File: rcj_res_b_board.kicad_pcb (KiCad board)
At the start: 2 copper layers, 92.5 x 100 mm, 94 parts, among them P1 GP2Y0A41SK0F, P10 SERVO0, P11 MPU9250, P12 PING0, P13 CONN_01X03, P14 CONN_01X03, P15 CONN_01X04, P16 CONN_02X04, P2 GP2Y0A41SK0F, P3 GP2Y0A41SK0F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

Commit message: Power routing & prep for autoroute
Moved some components to make routing power easier (net ties)
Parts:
- NT2, NT3, NT4: moved to B.Cu
- moved NT3 36.2 mm to (45.0, 67.5)
- moved NT4 35.2 mm to (47.0, 69.0)
- moved NT2 32.8 mm to (47.0, 65.0), turned to 180 degrees
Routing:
- net /3.3V: track 26.8 -> 251.0 mm, vias 0 -> 3
- net GNDD: track 88.1 -> 305.1 mm, vias 1 -> 2
- net GNDA: track 7.82 -> 121.7 mm, vias 1 -> 0
- net GNDPWR: track 50.1 -> 109.1 mm
- net /VBAT1: track 12.8 -> 61.5 mm, vias 0 -> 1
- net Net-(C23-Pad1): track 0.00 -> 4.11 mm
- net Net-(C22-Pad1): track 0.00 -> 3.40 mm
- net Net-(C21-Pad1): track 0.00 -> 3.40 mm
- net GND: track 44.7 -> 42.7 mm

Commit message: Changed grounds
Servo now uses digital ground
Battery monitor uses analog ground
Moved P_PWR1's 3.3V (used for debugging) to debug header
	P_PWR2 -> P_PWR1
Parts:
- removed the P_PWR1 at (89.0, 117.0)
- P_DBG1: value CONN_01X03 -> CONN_01X04; footprint Socket_Strips:Socket_Strip_Straight_1x03 -> Socket_Strips:Socket_Strip_Straight_1x04
- renumbered P_PWR2 to P_PWR1
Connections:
- MCU1 pad 1: Net-(MCU1-Pad1) -> (no net)
- MCU1 pad 15: Net-(MCU1-Pad15) -> (no net)
- MCU1 pad 2: Net-(MCU1-Pad2) -> (no net)
- MCU1 pad 20: Net-(MCU1-Pad20) -> (no net)
- MCU1 pad 36: Net-(MCU1-Pad36) -> (no net)
- MCU1 pad 40: Net-(MCU1-Pad40) -> (no net)
- MCU1 pad 5: Net-(MCU1-Pad5) -> (no net)
- MCU1 pad 53: Net-(MCU1-Pad53) -> (no net)
- MCU1 pad 56: Net-(MCU1-Pad56) -> (no net)
- MCU1 pad 6: Net-(MCU1-Pad6) -> (no net)
- MCU1 pad 62: Net-(MCU1-Pad62) -> (no net)
- P10 pad 1: GNDPWR -> GNDD
- P16 pad 8: Net-(P16-Pad8) -> (no net)
- P_CT1 pad 8: Net-(P_CT1-Pad8) -> (no net)
- P_DBG1 pad 2: /SWDIO -> /3.3V
- P_DBG1 pad 3: /SWCLK -> /SWDIO
- R8 pad 2: GNDD -> GNDA
- REG1 pad 4: Net-(REG1-Pad4) -> (no net)
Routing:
- net GNDPWR: track 109.1 -> 50.1 mm
- net GNDD: track 305.1 -> 269.9 mm
- net /VBAT1: track 61.5 -> 49.1 mm, vias 1 -> 0
- net /3.3V: track 251.0 -> 240.0 mm

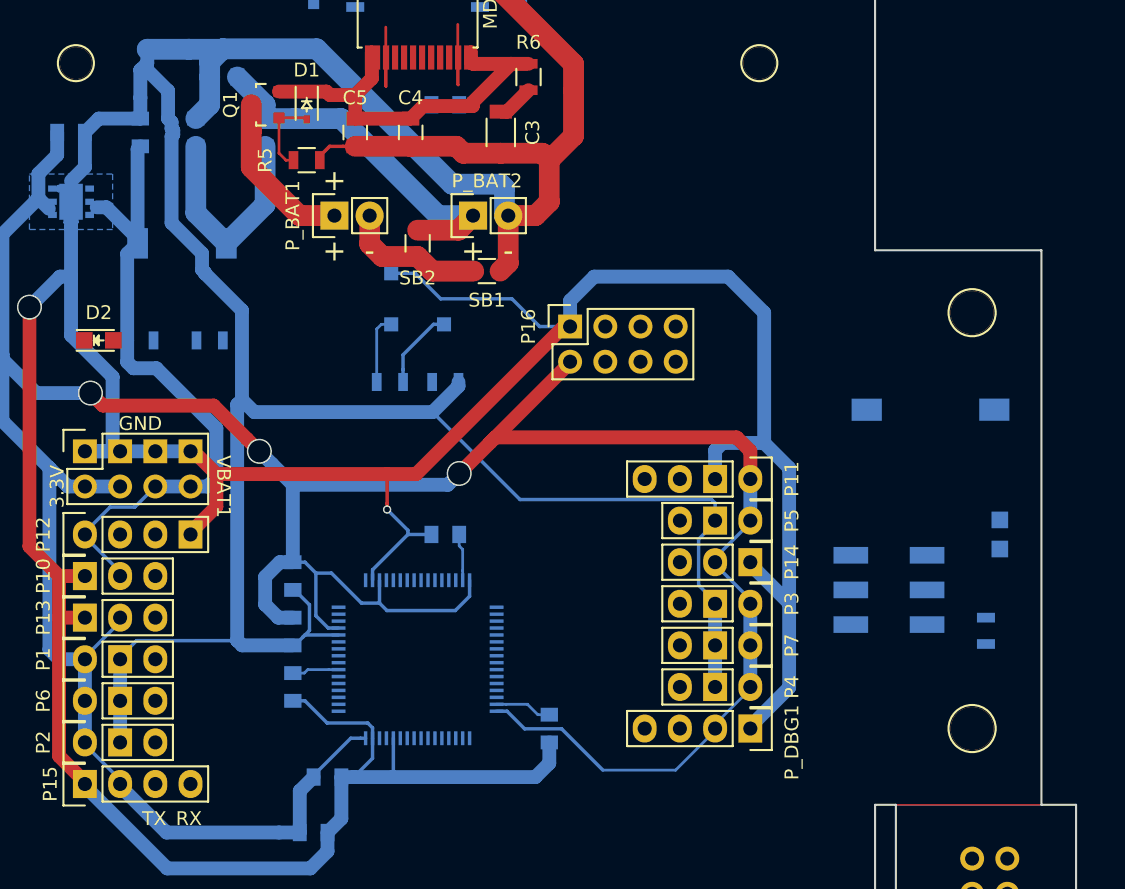
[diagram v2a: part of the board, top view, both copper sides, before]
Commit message: Re-routed power
Removed unnecessary wiring that wasn't power (to let autorouter route instead)
Misc fixes
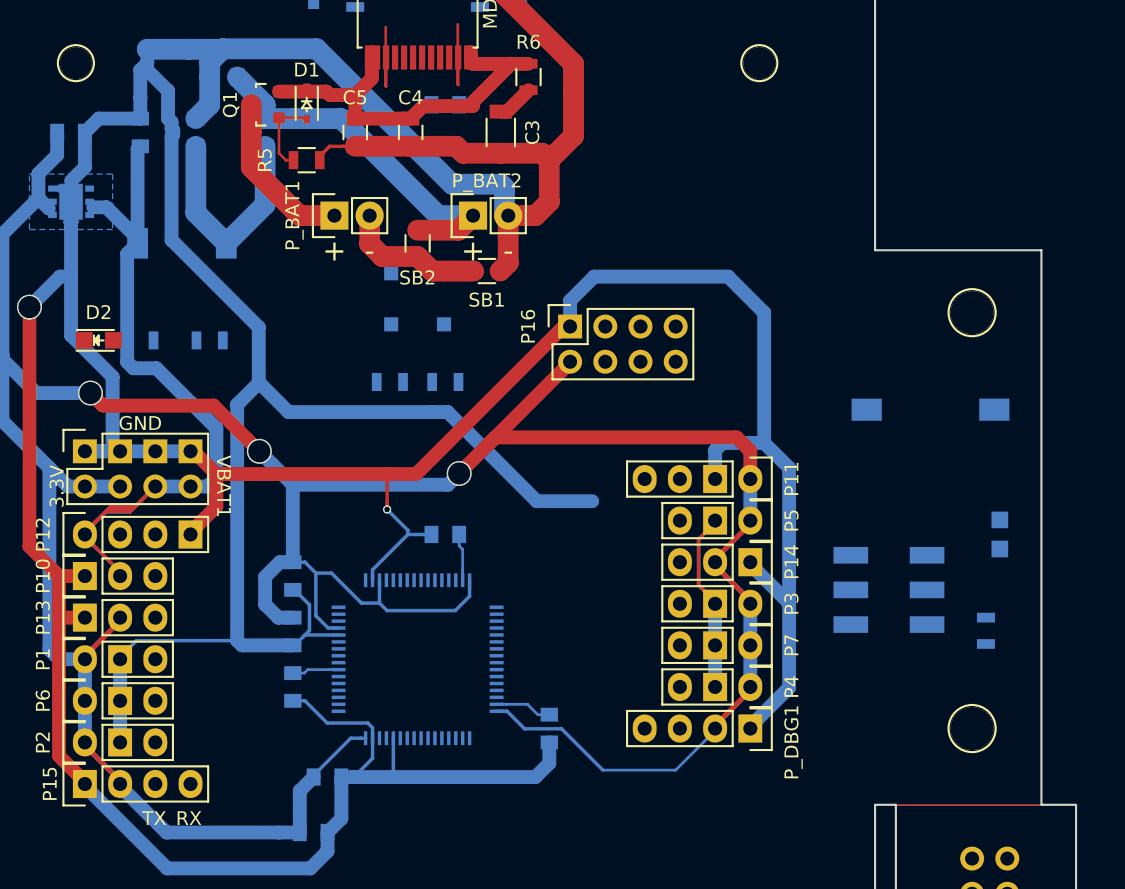
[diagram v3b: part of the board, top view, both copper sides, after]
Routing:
- net /3.3V: track 240.0 -> 295.0 mm
- net /VBAT1: track 49.1 -> 76.0 mm
- net GNDD: track 269.9 -> 255.4 mm
- net GNDA: track 121.9 -> 116.1 mm
- net Net-(R9-Pad2): track 5.01 -> 0.00 mm

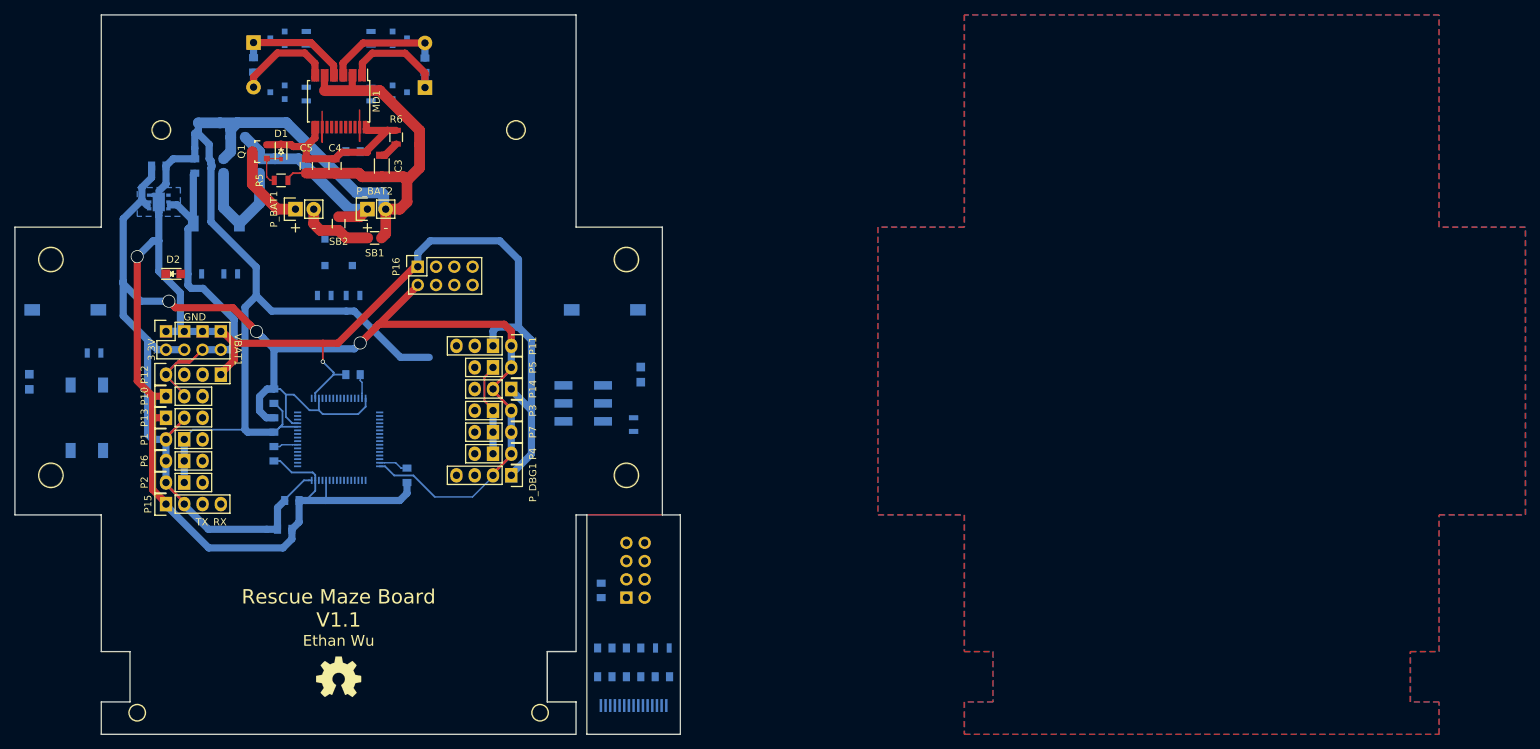
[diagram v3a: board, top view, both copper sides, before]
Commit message: Routed
Fixed offset / misplaced zone outline
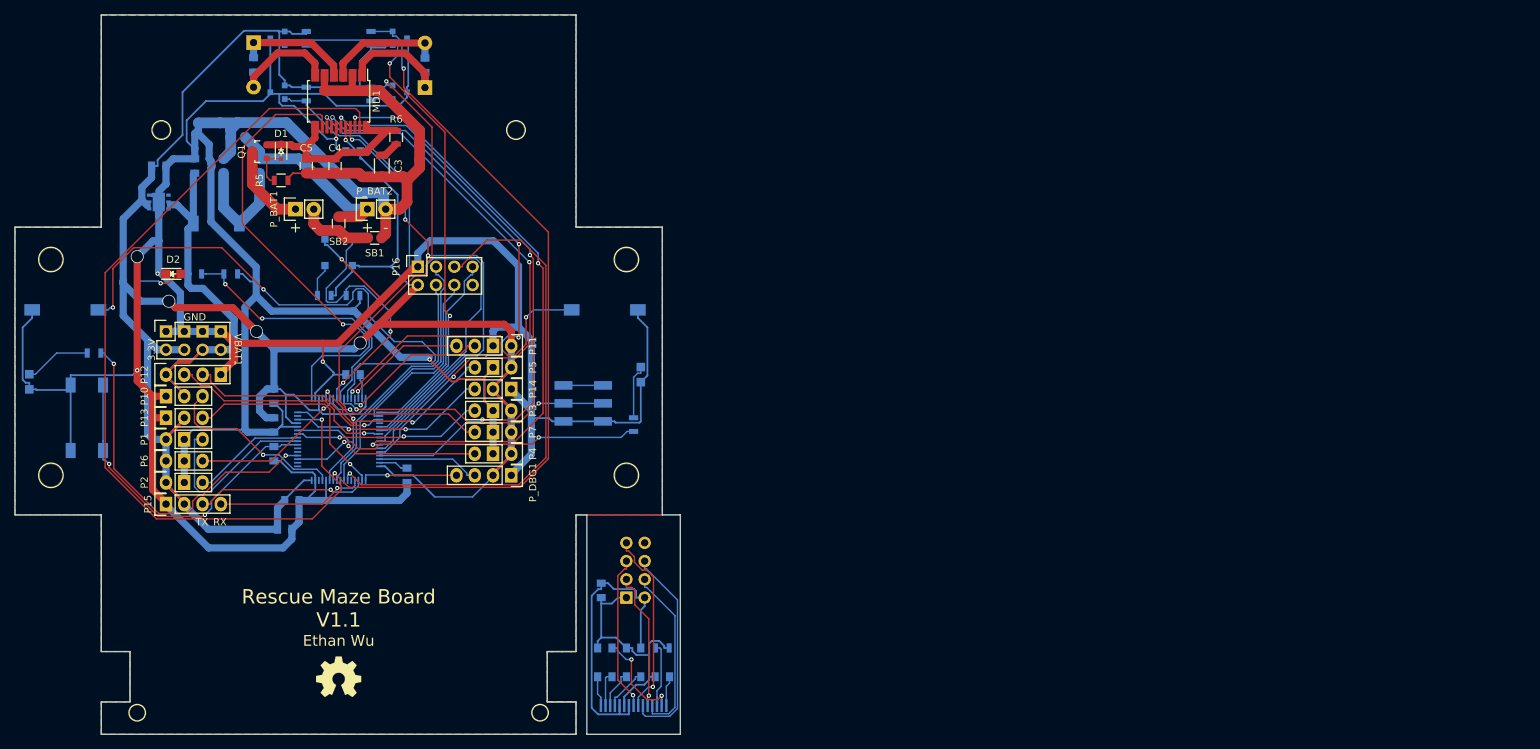
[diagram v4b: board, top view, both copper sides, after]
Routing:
- net GNDD: track 255.4 -> 408.2 mm, vias 2 -> 6
- net /MD_APWM: track 6.36 -> 126.3 mm, vias 0 -> 1
- net /3.3V: track 295.0 -> 400.1 mm, vias 3 -> 4
- net /M1_ENC_A: track 0.00 -> 104.9 mm, vias 0 -> 2
- net /MD_AIN2: track 0.00 -> 83.6 mm, vias 0 -> 3
- net /MD_STBY: track 0.00 -> 81.1 mm, vias 0 -> 3
- net /SW_USR1: track 0.00 -> 80.9 mm, vias 0 -> 2
- net /M0_ENC_A: track 0.00 -> 78.7 mm, vias 0 -> 2
- net /MD_BIN2: track 0.00 -> 77.1 mm, vias 0 -> 3
- net /M0_ENC_B: track 0.00 -> 76.5 mm
- net /MD_BIN1: track 0.00 -> 75.1 mm, vias 0 -> 3
- net /OLED_SS: track 0.00 -> 73.2 mm, vias 0 -> 1
- net /M1_ENC_B: track 0.00 -> 70.1 mm, vias 0 -> 2
- net /MD_AIN1: track 0.00 -> 63.3 mm, vias 0 -> 3
- net /MD_BPWM: track 6.36 -> 64.1 mm, vias 0 -> 1
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- added copper zone on F.Cu, net GNDD
- removed copper zone on B.Cu, net (none)
- removed copper zone on F.Cu, net (none)

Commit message: Added thermal vias
Final cleanup
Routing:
- net GNDD: track 408.2 -> 416.1 mm, vias 6 -> 16
- net /MD_APWM: track 126.3 -> 125.7 mm
- added copper zone on F.Cu, net GNDPWR
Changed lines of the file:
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@@
     (links 227)
     (no_connects 0)
-    (area 18.825 28.15 176.714286 188.100001)
+    (area 19.924999 49.924999 112.575001 150.100001)
     (thickness 1.6)
     (drawings 51)
-    (tracks 1319)
+    (tracks 1335)
     (zones 0)
     (modules 93)
@@
   (segment (start 56.484 77) (end 53.0018 73.5178) (width 1.5) (layer F.Cu) (net 1))
   (segment (start 59 77) (end 56.484 77) (width 1.5) (layer F.Cu) (net 1))
+  (segment (start 41.5 79) (end 40.5 80) (width 0.25) (layer B.Cu) (net 2))
+  (via (at 40.5 80) (size 0.6) (drill 0.4) (layers F.Cu B.Cu) (net 2))
+  (segment (start 40.425 76.65) (end 40.425 77.925) (width 0.25) (layer B.Cu) (net 2))
+  (via (at 41.5 79) (size 0.6) (drill 0.4) (layers F.Cu B.Cu) (net 2))
+  (segment (start 40.425 77.925) (end 41.5 79) (width 0.25) (layer B.Cu) (net 2))
+  (segment (start 38.5 78.5) (end 37.5 79.5) (width 0.25) (layer B.Cu) (net 2))
+  (via (at 37.5 79.5) (size 0.6) (drill 0.4) (layers F.Cu B.Cu) (net 2))
+  (segment (start 39.575 77.425) (end 38.5 78.5) (width 0.25) (layer B.Cu) (net 2))
+  (via (at 38.5 78.5) (size 0.6) (drill 0.4) (layers F.Cu B.Cu) (net 2))
+  (segment (start 39.575 76.65) (end 39.575 77.425) (width 0.25) (layer B.Cu) (net 2))
+  (via (at 41 73.5) (size 0.6) (drill 0.4) (layers F.Cu B.Cu) (net 2))
+  (via (at 40 74.5) (size 0.6) (drill 0.4) (layers F.Cu B.Cu) (net 2))
+  (via (at 40.425 76.65) (size 0.6) (drill 0.4) (layers F.Cu B.Cu) (net 2))
+  (via (at 39.575 76.65) (size 0.6) (drill 0.4) (layers F.Cu B.Cu) (net 2))
+  (via (at 40.425 75.35) (size 0.6) (drill 0.4) (layers F.Cu B.Cu) (net 2))
+  (via (at 39.575 75.35) (size 0.6) (drill 0.4) (layers F.Cu B.Cu) (net 2))
   (segment (start 76 85) (end 76 83.1364) (width 1) (layer B.Cu) (net 2))
   (segment (start 76 83.1364) (end 77.7364 81.4) (width 1) (layer B.Cu) (net 2))
@@
   (segment (start 54.5063 111.1548) (end 56.719 111.1548) (width 0.2) (layer B.Cu) (net 28))
   (segment (start 62.75 114.7) (end 62.75 113.9497) (width 0.2) (layer B.Cu) (net 28))
-  (segment (start 67.925 65.6) (end 67.925 63.5677) (width 0.2) (layer F.Cu) (net 29))
-  (segment (start 55.3677 63.0116) (end 32.5452 85.8341) (width 0.2) (layer F.Cu) (net 29))
-  (segment (start 65.3672 115.4127) (end 62.6657 112.7112) (width 0.2) (layer F.Cu) (net 29))
-  (segment (start 67.925 63.5677) (end 67.3689 63.0116) (width 0.2) (layer F.Cu) (net 29))
-  (segment (start 67.3689 63.0116) (end 55.3677 63.0116) (width 0.2) (layer F.Cu) (net 29))
+  (segment (start 67.925 65.6) (end 67.925 64.032723) (width 0.2) (layer F.Cu) (net 29))
+  (segment (start 67.33283 63.440553) (end 54.938747 63.440553) (width 0.2) (layer F.Cu) (net 29))
+  (segment (start 54.938747 63.440553) (end 32.5452 85.8341) (width 0.2) (layer F.Cu) (net 29))
+  (segment (start 67.925 64.032723) (end 67.33283 63.440553) (width 0.2) (layer F.Cu) (net 29))
   (segment (start 32.5452 85.8341) (end 32.5452 112.9177) (width 0.2) (layer F.Cu) (net 29))
-  (segment (start 61.3323 120.0509) (end 65.3672 116.016) (width 0.2) (layer F.Cu) (net 29))
   (segment (start 32.5452 112.9177) (end 39.6784 120.0509) (width 0.2) (layer F.Cu) (net 29))
   (segment (start 39.6784 120.0509) (end 61.3323 120.0509) (width 0.2) (layer F.Cu) (net 29))
+  (segment (start 61.3323 120.0509) (end 65.3672 116.016) (width 0.2) (layer F.Cu) (net 29))
   (segment (start 65.3672 116.016) (end 65.3672 115.4127) (width 0.2) (layer F.Cu) (net 29))
+  (segment (start 65.3672 115.4127) (end 62.6657 112.7112) (width 0.2) (layer F.Cu) (net 29))
   (segment (start 62.6657 112.7112) (end 62.6657 106.2547) (width 0.2) (layer F.Cu) (net 29))
   (via (at 62.6657 106.2547) (size 0.6) (layers F.Cu B.Cu) (net 29))
@@
     (polygon
       (pts
-        (xy 32 50) (xy 32 79.5) (xy 20 79.5) (xy 20 119.5) (xy 32 119.5)
-        (xy 32 138.5) (xy 36 138.5) (xy 36 145.5) (xy 32 145.5) (xy 32 150)
-        (xy 98 150) (xy 98 145.5) (xy 94 145.5) (xy 94 138.5) (xy 98 138.5)
-        (xy 98 119.5) (xy 110 119.5) (xy 110 79.5) (xy 98 79.5) (xy 98 50)
+        (xy 98 79.5) (xy 110 79.5) (xy 110 119.5) (xy 98 119.5) (xy 98 138.5)
+        (xy 94 138.5) (xy 94 145.5) (xy 98 145.5) (xy 98 150) (xy 32 150)
+        (xy 32 145.5) (xy 36 145.5) (xy 36 138.5) (xy 32 138.5) (xy 32 119.5)
+        (xy 20 119.5) (xy 20 79.5) (xy 32 79.5) (xy 32 50) (xy 98 50)
+        (xy 98 79.5)
+      )
+    )
+    (polygon
+      (pts        (xy 59 56.5) (xy 59 67.5) (xy 71 67.5) (xy 71 56.5)
       )
     )
@@
       )
     )
+  )
+  (zone (net 27) (net_name GNDPWR) (layer F.Cu) (hatch edge 0.508)
+    (connect_pads yes (clearance 0.508))
+    (min_thickness 0.254)
+    (fill yes (arc_segments 16) (thermal_gap 0.508) (thermal_bridge_width 0.508))
+    (polygon
+      (pts
+        (xy 60 57) (xy 70 57) (xy 70 66.5) (xy 60 66.5)
+      )
+    )
